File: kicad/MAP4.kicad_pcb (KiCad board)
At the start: 2 copper layers, 49.8 x 48.9 mm, 14 parts, among them P1 Logo_MA, P2 Pin, P3 Pin, P4 Pin, P5 Pin, P6 Pin

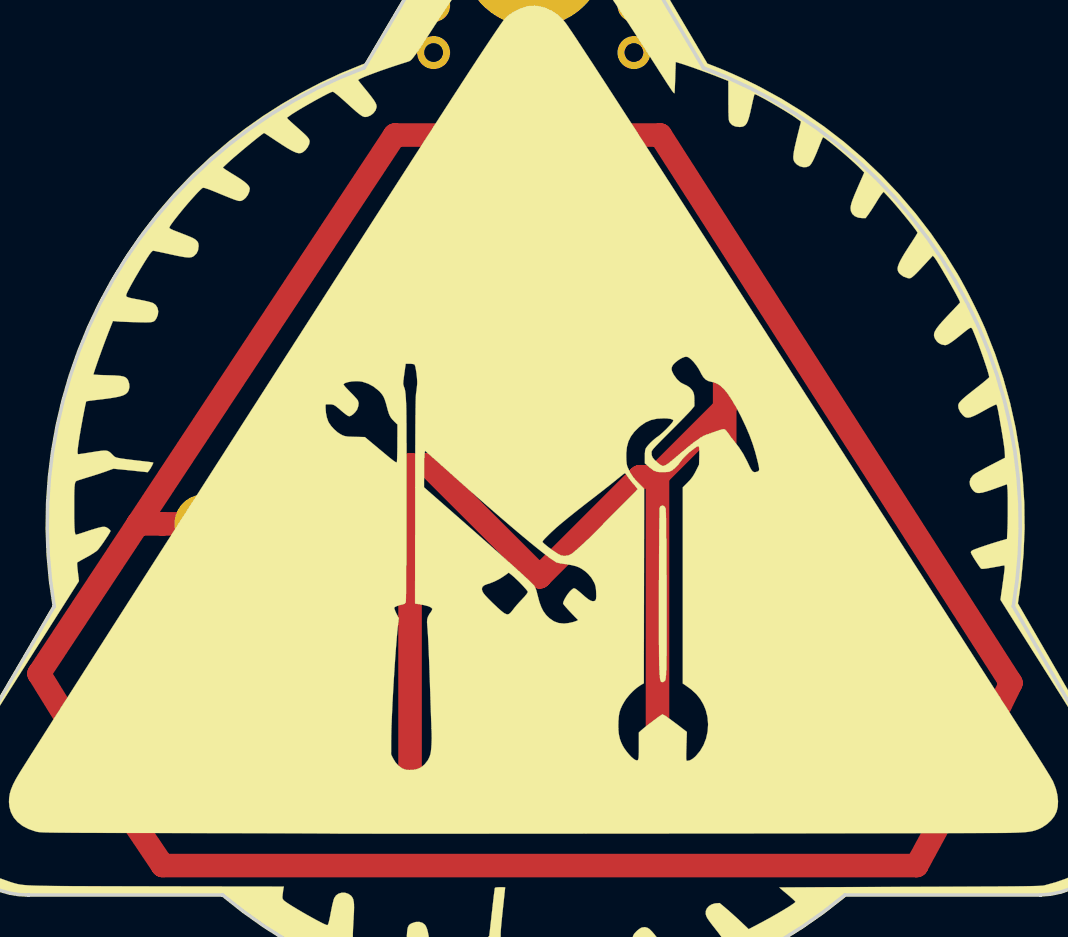
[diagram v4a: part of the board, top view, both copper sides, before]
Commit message: rev4 of MAP4 with battery holderfootprint fixed and minor track changes
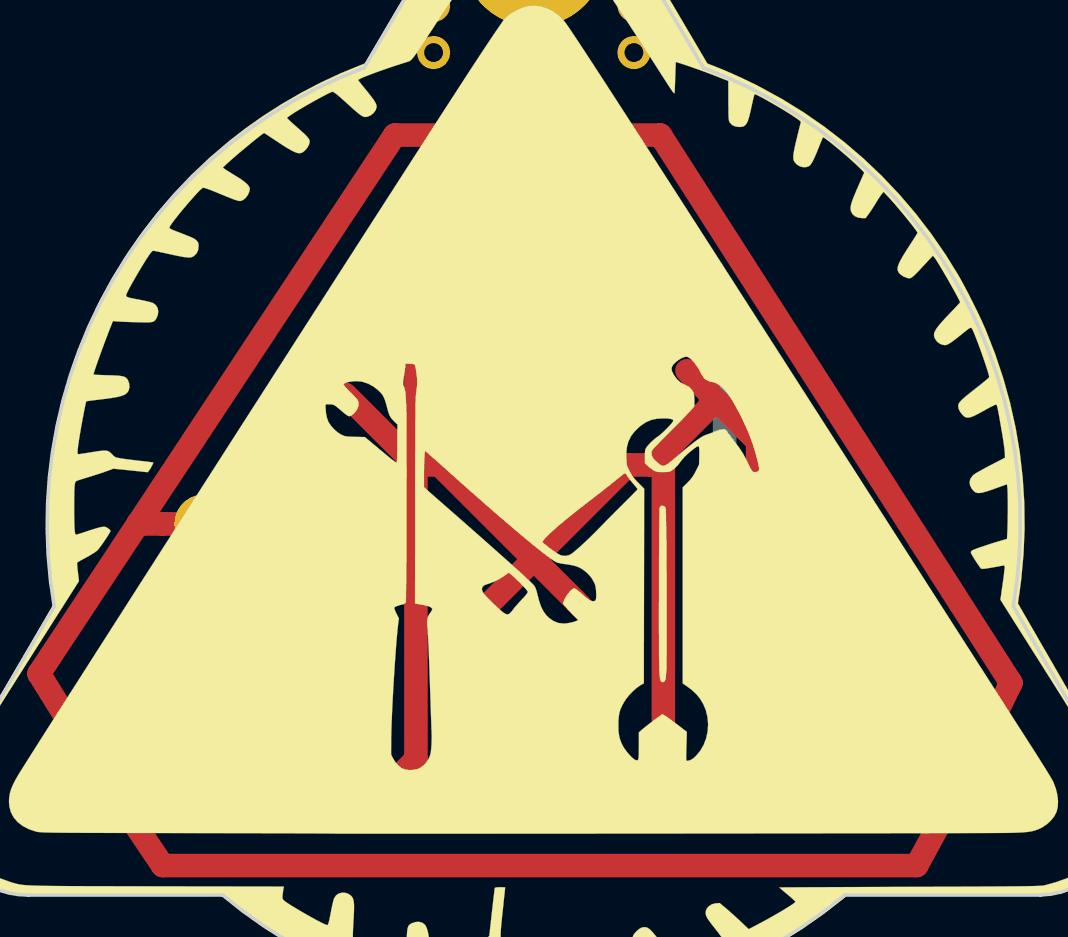
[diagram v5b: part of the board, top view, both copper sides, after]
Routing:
- net /GND: track 94.7 -> 127.0 mm
- net /LED_grn: track 13.5 -> 8.98 mm
- net /LED_blu: track 13.5 -> 8.98 mm
- net /LED_red: track 13.2 -> 9.31 mm
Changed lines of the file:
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@@
-(kicad_pcb (version 4) (host pcbnew 4.1.0-alpha+201606040946+6883~45~ubuntu15.10.1-product)
+(kicad_pcb (version 4) (host pcbnew 4.1.0-alpha+201607271302+6994~46~ubuntu16.04.1-product)
   (general
     (links 17)
-    (no_connects 6)
+    (no_connects 0)
     (area 111.5 71.26989 175.153445 126.745)
     (thickness 1.6)
     (drawings 25)
-    (tracks 59)
+    (tracks 64)
     (zones 0)
     (modules 14)
@@
     (visible_elements FFFFFF7F)
     (pcbplotparams
-      (layerselection 0x00130_ffffffff)
-      (usegerberextensions false)
+      (layerselection 0x010f0_ffffffff)
+      (usegerberextensions true)
+      (usegerberattributes true)
       (excludeedgelayer false)
       (linewidth 0.050800)
-      (plotframeref true)
+      (plotframeref false)
       (viasonmask false)
       (mode 1)
-      (useauxorigin false)
+      (useauxorigin true)
       (hpglpennumber 1)
       (hpglpenspeed 20)
@@
       (plotvalue true)
       (plotinvisibletext false)
-      (padsonsilk true)
-      (subtractmaskfromsilk false)
-      (outputformat 4)
+      (padsonsilk false)
+      (subtractmaskfromsilk true)
+      (outputformat 1)
       (mirror false)
-      (drillshape 2)
+      (drillshape 0)
       (scaleselection 1)
-      (outputdirectory pdf/))
+      (outputdirectory gerber/))
   )
   (net 0 "")
@@
     (descr "SMT capacitor, 0805")
     (attr smd)
-    (fp_text reference R3 (at -2.032 0 390) (layer B.SilkS)
+    (fp_text reference R3 (at -2.032 0 30) (layer B.SilkS)
       (effects (font (size 0.635 0.889) (thickness 0.1143)) (justify mirror))
     )
@@
       (effects (font (size 0.8 0.8) (thickness 0.15)))
     )
-    (fp_text user SHRT (at 1.27 -5.08 360) (layer B.SilkS)
+    (fp_text user SHRT (at 1.27 -5.08) (layer B.SilkS)
       (effects (font (size 1 1) (thickness 0.2)) (justify mirror))
     )
-    (fp_text user LONG (at -1.27 -5.08 360) (layer B.SilkS)
+    (fp_text user LONG (at -1.27 -5.08) (layer B.SilkS)
       (effects (font (size 1 1) (thickness 0.2)) (justify mirror))
     )
@@
   (segment (start 166.25 114.5) (end 134.25 114.5) (width 1) (layer F.Cu) (net 1))
   (segment (start 134.25 114.5) (end 131.650148 110.635) (width 1) (layer F.Cu) (net 1) (status 20))
-  (segment (start 158.1 100) (end 158.1 95.1) (width 1) (layer F.Cu) (net 2))
-  (segment (start 158.1 95.1) (end 158.1 92.1) (width 1) (layer F.Cu) (net 2))
-  (segment (start 155.25 98) (end 155.25 97.95) (width 1) (layer F.Cu) (net 2))
-  (segment (start 155.25 97.95) (end 158.1 95.1) (width 1) (layer F.Cu) (net 2))
-  (segment (start 158.1 92.1) (end 157.25 91.25) (width 1) (layer F.Cu) (net 2))
+  (segment (start 159.5 96.5) (end 159.5 97.5) (width 1) (layer F.Cu) (net 2))
+  (segment (start 159 96) (end 159.5 96.5) (width 1) (layer F.Cu) (net 2))
+  (segment (start 157.5 94.5) (end 159 96) (width 1) (layer F.Cu) (net 2))
+  (segment (start 157.5 94.5) (end 156.5 93.5) (width 1) (layer F.Cu) (net 2))
+  (segment (start 157.5 95) (end 157.5 94.5) (width 1) (layer F.Cu) (net 2))
+  (segment (start 145 97.5) (end 142 94.5) (width 1) (layer F.Cu) (net 2))
+  (segment (start 155 97.5) (end 155.5 97.5) (width 1) (layer F.Cu) (net 2))
+  (segment (start 154 97.5) (end 155 97.5) (width 1) (layer F.Cu) (net 2))
+  (segment (start 155 97.5) (end 157.5 95) (width 1) (layer F.Cu) (net 2))
+  (segment (start 150 101.5) (end 148 103.5) (width 1) (layer F.Cu) (net 2))
+  (segment (start 150 101.5) (end 152 103.5) (width 1) (layer F.Cu) (net 2))
+  (segment (start 145 97.5) (end 146 97.5) (width 1) (layer F.Cu) (net 2))
+  (segment (start 156.519527 111.019527) (end 161.468 111.019527) (width 1) (layer F.Cu) (net 2))
+  (segment (start 146 97.5) (end 150 101.5) (width 1) (layer F.Cu) (net 2))
+  (segment (start 150 101.5) (end 154 97.5) (width 1) (layer F.Cu) (net 2))
+  (segment (start 155.5 97.5) (end 155.5 110) (width 1) (layer F.Cu) (net 2))
+  (segment (start 155.5 110) (end 156.519527 111.019527) (width 1) (layer F.Cu) (net 2))
+  (segment (start 145 97.5) (end 145 93.5) (width 1) (layer F.Cu) (net 2))
+  (segment (start 145 110) (end 145 97.5) (width 1) (layer F.Cu) (net 2))
+  (segment (start 143.980473 111.019527) (end 145 110) (width 1) (layer F.Cu) (net 2))
+  (segment (start 138.532 111.019527) (end 143.980473 111.019527) (width 1) (layer F.Cu) (net 2))
+  (segment (start 158.1 110.1) (end 159.019527 111.019527) (width 1) (layer B.Cu) (net 2))
+  (segment (start 159.019527 111.019527) (end 161.468 111.019527) (width 1) (layer B.Cu) (net 2))
+  (segment (start 158.1 100) (end 158.1 110.1) (width 1) (layer B.Cu) (net 2))
+  (segment (start 158.1 100) (end 158.1 92.1) (width 1) (layer B.Cu) (net 2))
+  (segment (start 158.1 92.1) (end 157 91) (width 1) (layer B.Cu) (net 2))
+  (segment (start 157 91) (end 147 91) (width 1) (layer B.Cu) (net 2))
+  (segment (start 147 91) (end 145.936 89.936) (width 1) (layer B.Cu) (net 2))
+  (segment (start 145.936 89.936) (end 145.936 87.75) (width 1) (layer B.Cu) (net 2))
+  (segment (start 149.05 87.75) (end 145.936 87.75) (width 1) (layer B.Cu) (net 2))
+  (segment (start 161.468 111.019527) (end 161.468 109.879724) (width 1) (layer B.Cu) (net 2))
+  (segment (start 161.468 109.879724) (end 163.025 108.322724) (width 1) (layer B.Cu) (net 2))
+  (segment (start 138.532 111.019527) (end 138.532 109.879724) (width 1) (layer B.Cu) (net 2))
+  (segment (start 138.532 109.879724) (end 136.975 108.322724) (width 1) (layer B.Cu) (net 2))
   (segment (start 158.1 100) (end 163 100) (width 1) (layer B.Cu) (net 2))
-  (segment (start 161.468 111.019527) (end 155.769527 111.019527) (width 1) (layer F.Cu) (net 2))
-  (segment (start 161.468 111.019527) (end 161.468 109.879724) (width 1) (layer F.Cu) (net 2))
-  (segment (start 161.468 109.879724) (end 163.025 108.322724) (width 1) (layer F.Cu) (net 2))
-  (segment (start 155.769527 111.019527) (end 155.25 110.5) (width 1) (layer F.Cu) (net 2))
-  (segment (start 155.25 110.5) (end 155.25 98) (width 1) (layer F.Cu) (net 2))
-  (segment (start 154.5 98) (end 155.25 98) (width 1) (layer F.Cu) (net 2))
-  (segment (start 145.936 87.75) (end 145.936 90.186) (width 1) (layer F.Cu) (net 2))
-  (segment (start 145.936 90.186) (end 147 91.25) (width 1) (layer F.Cu) (net 2))
-  (segment (start 147 91.25) (end 157.25 91.25) (width 1) (layer F.Cu) (net 2))
-  (segment (start 145.936 87.75) (end 149.05 87.75) (width 1) (layer F.Cu) (net 2) (status 30))
-  (segment (start 138.532 111.019527) (end 144.230473 111.019527) (width 1) (layer F.Cu) (net 2))
-  (segment (start 138.532 111.019527) (end 138.532 109.879724) (width 1) (layer F.Cu) (net 2))
-  (segment (start 138.532 109.879724) (end 136.975 108.322724) (width 1) (layer F.Cu) (net 2))
-  (segment (start 144.230473 111.019527) (end 144.75 110.5) (width 1) (layer F.Cu) (net 2))
-  (segment (start 144.75 110.5) (end 144.75 97.5) (width 1) (layer F.Cu) (net 2))
-  (segment (start 144.75 97.5) (end 145.5 97.5) (width 1) (layer F.Cu) (net 2))
-  (segment (start 145.5 97.5) (end 150.25 102.25) (width 1) (layer F.Cu) (net 2))
-  (segment (start 150.25 102.25) (end 154.5 98) (width 1) (layer F.Cu) (net 2))
+  (segment (start 150.95 87.75) (end 154.064 87.75) (width 1) (layer B.Cu) (net 3))
   (segment (start 150 84.27) (end 151.77 84.27) (width 1) (layer B.Cu) (net 3))
   (segment (start 154.064 86.564) (end 154.064 87.75) (width 1) (layer B.Cu) (net 3))
   (segment (start 151.77 84.27) (end 154.064 86.564) (width 1) (layer B.Cu) (net 3))
-  (segment (start 150.95 87.75) (end 150.95 85.22) (width 1) (layer F.Cu) (net 3) (status 10))
-  (segment (start 150.95 85.22) (end 150 84.27) (width 1) (layer F.Cu) (net 3) (status 20))
-  (segment (start 154.064 87.75) (end 150.95 87.75) (width 1) (layer F.Cu) (net 3) (status 30))
+  (segment (start 163.975 106.677276) (end 163.975 105.537473) (width 1) (layer B.Cu) (net 4))
+  (segment (start 163.975 105.537473) (end 165.532 103.980473) (width 1) (layer B.Cu) (net 4))
   (segment (start 166.150148 109.365) (end 166.150148 104.598621) (width 1) (layer B.Cu) (net 4))
   (segment (start 166.150148 104.598621) (end 165.532 103.980473) (width 1) (layer B.Cu) (net 4))
-  (segment (start 166.150148 109.365) (end 166.150148 105.738424) (width 1) (layer F.Cu) (net 4))
-  (segment (start 166.150148 105.738424) (end 165.532 105.120276) (width 1) (layer F.Cu) (net 4))
-  (segment (start 165.532 103.980473) (end 165.532 105.120276) (width 1) (layer F.Cu) (net 4))
-  (segment (start 165.532 105.120276) (end 163.975 106.677276) (width 1) (layer F.Cu) (net 4))
+  (segment (start 136.025 106.677276) (end 136.025 105.537473) (width 1) (layer B.Cu) (net 5))
+  (segment (start 136.025 105.537473) (end 134.468 103.980473) (width 1) (layer B.Cu) (net 5))
   (segment (start 133.849852 104.598621) (end 134.468 103.980473) (width 1) (layer B.Cu) (net 5))
-  (segment (start 134.468 105.120276) (end 136.025 106.677276) (width 1) (layer F.Cu) (net 5))
-  (segment (start 134.468 103.980473) (end 134.468 105.120276) (width 1) (layer F.Cu) (net 5))
-  (segment (start 133.849852 105.738424) (end 134.468 105.120276) (width 1) (layer F.Cu) (net 5))
   (segment (start 133.849852 109.365) (end 133.849852 104.598621) (width 1) (layer B.Cu) (net 5))
-  (segment (start 133.849852 109.365) (end 133.849852 105.738424) (width 1) (layer F.Cu) (net 5))
 )

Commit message: minor edits to bottom silk layer for PCBpower ETOK mark issue
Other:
- board text added: "PLEASE ADD ETOK MARK TO BOTTOM LAYER ONLY IN THE PROVIDED BOX"
- board text added: "SPACE FOR ETOK MARK"
- board text removed: "SPACE FOR ETOK MARK AND CODE"
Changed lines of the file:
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@@
-(kicad_pcb (version 4) (host pcbnew 4.1.0-alpha+201607271302+6994~46~ubuntu16.04.1-product)
+(kicad_pcb (version 4) (host pcbnew 4.0.6-e0-6349~53~ubuntu16.04.1)
   (general
     (links 17)
     (no_connects 0)
-    (area 111.5 71.26989 175.153445 126.745)
+    (area 111.650001 71.26989 206.380001 126.7)
     (thickness 1.6)
-    (drawings 25)
+    (drawings 34)
     (tracks 64)
     (zones 0)
@@
     (aux_axis_origin 125 120.5)
     (grid_origin 125 120.5)
-    (visible_elements FFFFFF7F)
+    (visible_elements FFFFEF7F)
     (pcbplotparams
-      (layerselection 0x010f0_ffffffff)
-      (usegerberextensions true)
-      (usegerberattributes true)
+      (layerselection 0x00130_80000001)
+      (usegerberextensions false)
       (excludeedgelayer false)
       (linewidth 0.050800)
-      (plotframeref false)
+      (plotframeref true)
       (viasonmask false)
       (mode 1)
-      (useauxorigin true)
+      (useauxorigin false)
       (hpglpennumber 1)
       (hpglpenspeed 20)
       (hpglpendiameter 15)
+      (hpglpenoverlay 2)
       (psnegative false)
       (psa4output false)
@@
       (plotvalue true)
       (plotinvisibletext false)
-      (padsonsilk false)
-      (subtractmaskfromsilk true)
-      (outputformat 1)
+      (padsonsilk true)
+      (subtractmaskfromsilk false)
+      (outputformat 4)
       (mirror false)
-      (drillshape 0)
+      (drillshape 2)
       (scaleselection 1)
-      (outputdirectory gerber/))
+      (outputdirectory pdf/))
   )
   (net 0 "")
@@
     (descr "SMT capacitor, 0805")
     (attr smd)
-    (fp_text reference R3 (at -2.032 0 30) (layer B.SilkS)
+    (fp_text reference R3 (at -2.032 0 390) (layer B.SilkS)
       (effects (font (size 0.635 0.889) (thickness 0.1143)) (justify mirror))
     )
@@
     (descr "LED 5mm - Lead pitch 100mil (2,54mm)")
     (tags "LED led 5mm 5MM 100mil 2,54mm")
-    (fp_text reference D3 (at -0.008975 1.75 -150) (layer F.SilkS)
+    (fp_text reference D3 (at -0.008975 1.75 210) (layer F.SilkS)
       (effects (font (size 0.8 0.8) (thickness 0.15)))
     )
@@
     (descr "LED 5mm - Lead pitch 100mil (2,54mm)")
     (tags "LED led 5mm 5MM 100mil 2,54mm")
-    (fp_text reference D2 (at -0.008975 1.75 -30) (layer F.SilkS)
+    (fp_text reference D2 (at -0.008975 1.75 330) (layer F.SilkS)
       (effects (font (size 0.8 0.8) (thickness 0.15)))
     )
@@
     (descr "LED 5mm - Lead pitch 100mil (2,54mm)")
     (tags "LED led 5mm 5MM 100mil 2,54mm")
-    (fp_text reference D1 (at -0.008975 1.75 90) (layer F.SilkS)
+    (fp_text reference D1 (at -0.008975 1.75 450) (layer F.SilkS)
       (effects (font (size 0.8 0.8) (thickness 0.15)))
     )
@@
       (effects (font (size 0.8 0.8) (thickness 0.15)))
     )
-    (fp_text user SHRT (at 1.27 -5.08) (layer B.SilkS)
+    (fp_text user SHRT (at 1.27 -5.08 360) (layer B.SilkS)
       (effects (font (size 1 1) (thickness 0.2)) (justify mirror))
     )
-    (fp_text user LONG (at -1.27 -5.08) (layer B.SilkS)
+    (fp_text user LONG (at -1.27 -5.08 360) (layer B.SilkS)
       (effects (font (size 1 1) (thickness 0.2)) (justify mirror))
     )
@@
     )
   )
+  (gr_line (start 173.26 100.18) (end 171.99 98.91) (layer Dwgs.User) (width 0.2))
+  (gr_line (start 173.26 97.64) (end 173.26 100.18) (layer Dwgs.User) (width 0.2))
+  (gr_line (start 171.99 98.91) (end 173.26 97.64) (layer Dwgs.User) (width 0.2))
+  (gr_line (start 177.07 98.91) (end 171.99 98.91) (layer Dwgs.User) (width 0.2))
+  (gr_line (start 177.07 103.99) (end 177.07 93.83) (layer Dwgs.User) (width 0.2))
+  (gr_line (start 206.28 103.99) (end 177.07 103.99) (layer Dwgs.User) (width 0.2))
+  (gr_line (start 206.28 93.83) (end 206.28 103.99) (layer Dwgs.User) (width 0.2))
+  (gr_line (start 177.07 93.83) (end 206.28 93.83) (layer Dwgs.User) (width 0.2))
+  (gr_text "PLEASE ADD ETOK MARK\nTO BOTTOM LAYER ONLY\nIN THE PROVIDED BOX" (at 191.04 98.91) (layer Dwgs.User)
+    (effects (font (size 1.5 1.5) (thickness 0.3)))
+  )
   (gr_text "if it smells like chicken\nyou're holding it wrong !" (at 150 116) (layer B.SilkS)
     (effects (font (size 1 1) (thickness 0.2)) (justify mirror))
@@
   (gr_line (start 156 104.5) (end 144 104.5) (layer B.SilkS) (width 0.2))
   (gr_line (start 156 95.5) (end 156 104.5) (layer B.SilkS) (width 0.2))
-  (gr_text "SPACE FOR\nETOK MARK\nAND CODE" (at 150 93) (layer B.SilkS)
-    (effects (font (size 1 1) (thickness 0.2)) (justify mirror))
+  (gr_text "SPACE FOR\nETOK MARK" (at 150 93) (layer B.SilkS)
+    (effects (font (size 1.25 1.25) (thickness 0.25)) (justify mirror))
   )
   (dimension 49 (width 0.3) (layer Dwgs.User)
